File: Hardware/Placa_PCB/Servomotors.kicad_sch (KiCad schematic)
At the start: 12 parts, among them J4 Conn_01x03_Pin, J5 Conn_01x03_Pin, J6 Conn_01x03_Pin, J7 Conn_01x03_Pin

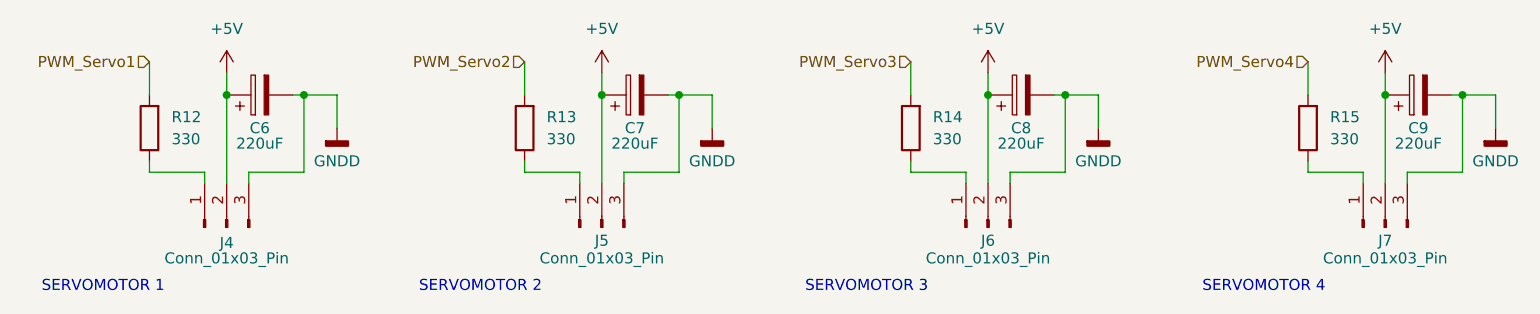
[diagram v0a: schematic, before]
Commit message: Agregando MCU al esquematico
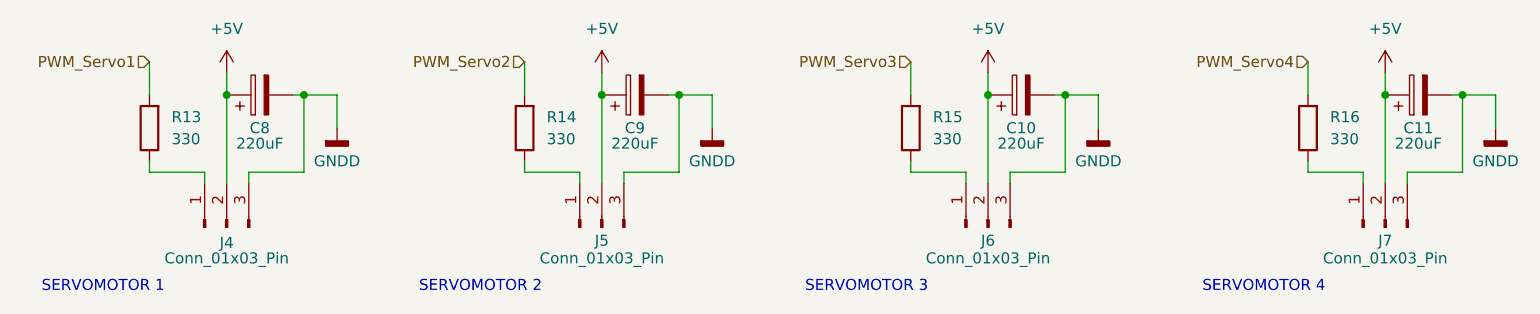
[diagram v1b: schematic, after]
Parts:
- renumbered C8 to C10, C9 to C11, C6 to C8, C7 to C9, R12 to R13, R13 to R14, R14 to R15, R15 to R16
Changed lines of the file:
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@@
+		(dnp no)
+		(fields_autoplaced yes)
+		(property "Reference" "R15"
+			(at 158.75 86.3599 0)
+			(effects
+				(font
+					(size 1.27 1.27)
+				)
+				(justify right)
+			)
+		)
+		(property "Value" "330"
+			(at 158.75 88.8999 0)
+			(effects
+				(font
+					(size 1.27 1.27)
+				)
+				(justify right)
+			)
+		)
+		(property "Footprint" "Resistor_SMD:R_0805_2012Metric_Pad1.20x1.40mm_HandSolder"
+			(at 157.988 87.63 90)
+			(effects
+				(font
+					(size 1.27 1.27)
+				)
+				(hide yes)
+			)
+		)
+		(property "Datasheet" "~"
+			(at 156.21 87.63 0)
+			(effects
+				(font
+					(size 1.27 1.27)
+				)
+				(hide yes)
+			)
+		)
+		(property "Description" "Resistor"
+			(at 156.21 87.63 0)
+			(effects
+				(font
+					(size 1.27 1.27)
+				)
+				(hide yes)
+			)
+		)
+		(pin "1"
+		)
+		(pin "2"
+		)
+		(instances
+			(project "ScramblerBot"
+				(path "/ca162c4b-e7f6-494c-9ea1-0d86ef4a8e44/0bfdb5c0-68d8-49ec-ac8d-698a51ef3bdb"
+					(reference "R15")
+					(unit 1)
+				)
+			)
+		)
+	)
+	(symbol
+		(lib_id "Device:R")
+		(at 201.93 87.63 180)
+		(unit 1)
+		(exclude_from_sim no)
+		(in_bom yes)
+		(on_board yes)
+		(dnp no)
+		(fields_autoplaced yes)
+		(property "Reference" "R16"
+			(at 204.47 86.3599 0)
+			(effects
+				(font
+					(size 1.27 1.27)
+				)
+				(justify right)
+			)
+		)
+		(property "Value" "330"
+			(at 204.47 88.8999 0)
+			(effects
+				(font
+					(size 1.27 1.27)
+				)
+				(justify right)
+			)
+		)
+		(property "Footprint" "Resistor_SMD:R_0805_2012Metric_Pad1.20x1.40mm_HandSolder"
+			(at 203.708 87.63 90)
+			(effects
+				(font
+					(size 1.27 1.27)
+				)
+				(hide yes)
+			)
+		)
+		(property "Datasheet" "~"
+			(at 201.93 87.63 0)
+			(effects
+				(font
+					(size 1.27 1.27)
+				)
+				(hide yes)
+			)
+		)
+		(property "Description" "Resistor"
+			(at 201.93 87.63 0)
+			(effects
+				(font
+					(size 1.27 1.27)
+				)
+				(hide yes)
+			)
+		)
+		(pin "1"
+		)
+		(pin "2"
+		)
+		(instances
+			(project "ScramblerBot"
+				(path "/ca162c4b-e7f6-494c-9ea1-0d86ef4a8e44/0bfdb5c0-68d8-49ec-ac8d-698a51ef3bdb"
+					(reference "R16")
+					(unit 1)
+				)
+			)
+		)
+	)
+	(symbol
+		(lib_id "Device:C_Polarized")
+		(at 214.63 83.82 90)
+		(unit 1)
+		(exclude_from_sim no)
+		(in_bom yes)
+		(on_board yes)
+		(dnp no)
+		(property "Reference" "C11"
+			(at 214.63 87.63 90)
+			(effects
+				(font
+					(size 1.27 1.27)
+				)
+			)
+		)
+		(property "Value" "220uF"
+			(at 214.63 89.408 90)
+			(effects
+				(font
+					(size 1.27 1.27)
+				)
+			)
+		)
+		(property "Footprint" "Capacitor_SMD:CP_Elec_6.3x7.7"
+			(at 218.44 82.8548 0)
+			(effects
+				(font
+					(size 1.27 1.27)
+				)
+				(hide yes)
+			)
+		)
+		(property "Datasheet" "~"
+			(at 214.63 83.82 0)
+			(effects
+				(font
+					(size 1.27 1.27)
+				)
+				(hide yes)
+			)
+		)
+		(property "Description" "Polarized capacitor"
+			(at 214.63 83.82 0)
+			(effects
+				(font
+					(size 1.27 1.27)
+				)
+				(hide yes)
+			)
+		)
+		(pin "1"
+		)
+		(pin "2"
+		)
+		(instances
+			(project "ScramblerBot"
+				(path "/ca162c4b-e7f6-494c-9ea1-0d86ef4a8e44/0bfdb5c0-68d8-49ec-ac8d-698a51ef3bdb"
+					(reference "C11")
+					(unit 1)
+				)
+			)
+		)
+	)
+	(symbol
+		(lib_id "Device:R")
+		(at 111.76 87.63 180)
+		(unit 1)
+		(exclude_from_sim no)
+		(in_bom yes)
+		(on_board yes)
 		(dnp no)
 		(fields_autoplaced yes)
 		(property "Reference" "R14"
-			(at 158.75 86.3599 0)
-			(effects
-				(font
-					(size 1.27 1.27)
-				)
-				(justify right)
-			)
-		)
-		(property "Value" "330"
-			(at 158.75 88.8999 0)
-			(effects
-				(font
-					(size 1.27 1.27)
-				)
-				(justify right)
-			)
-		)
-		(property "Footprint" "Resistor_SMD:R_0805_2012Metric_Pad1.20x1.40mm_HandSolder"
-			(at 157.988 87.63 90)
-			(effects
-				(font
-					(size 1.27 1.27)
-				)
-				(hide yes)
-			)
-		)
-		(property "Datasheet" "~"
-			(at 156.21 87.63 0)
-			(effects
-				(font
-					(size 1.27 1.27)
-				)
-				(hide yes)
-			)
-		)
-		(property "Description" "Resistor"
-			(at 156.21 87.63 0)
-			(effects
-				(font
-					(size 1.27 1.27)
-				)
-				(hide yes)
-			)
-		)
-		(pin "1"
-		)
-		(pin "2"
-		)
-		(instances
-			(project "ScramblerBot"
-				(path "/ca162c4b-e7f6-494c-9ea1-0d86ef4a8e44/0bfdb5c0-68d8-49ec-ac8d-698a51ef3bdb"
-					(reference "R14")
-					(unit 1)
-				)
-			)
-		)
-	)
-	(symbol
-		(lib_id "Device:R")
-		(at 201.93 87.63 180)
-		(unit 1)
-		(exclude_from_sim no)
-		(in_bom yes)
-		(on_board yes)
-		(dnp no)
-		(fields_autoplaced yes)
-		(property "Reference" "R15"
-			(at 204.47 86.3599 0)
-			(effects
-				(font
-					(size 1.27 1.27)
-				)
-				(justify right)
-			)
-		)
-		(property "Value" "330"
-			(at 204.47 88.8999 0)
-			(effects
-				(font
-					(size 1.27 1.27)
-				)
-				(justify right)
-			)
-		)
-		(property "Footprint" "Resistor_SMD:R_0805_2012Metric_Pad1.20x1.40mm_HandSolder"
-			(at 203.708 87.63 90)
-			(effects
-				(font
-					(size 1.27 1.27)
-				)
-				(hide yes)
-			)
-		)
-		(property "Datasheet" "~"
-			(at 201.93 87.63 0)
-			(effects
-				(font
-					(size 1.27 1.27)
-				)
-				(hide yes)
-			)
-		)
-		(property "Description" "Resistor"
-			(at 201.93 87.63 0)
-			(effects
-				(font
-					(size 1.27 1.27)
-				)
-				(hide yes)
-			)
-		)
-		(pin "1"
-		)
-		(pin "2"
-		)
-		(instances
-			(project "ScramblerBot"
-				(path "/ca162c4b-e7f6-494c-9ea1-0d86ef4a8e44/0bfdb5c0-68d8-49ec-ac8d-698a51ef3bdb"
-					(reference "R15")
-					(unit 1)
-				)
-			)
-		)
-	)
-	(symbol
-		(lib_id "Device:C_Polarized")
-		(at 214.63 83.82 90)
-		(unit 1)
-		(exclude_from_sim no)
-		(in_bom yes)
-		(on_board yes)
-		(dnp no)
-		(property "Reference" "C9"
-			(at 214.63 87.63 90)
-			(effects
-				(font
-					(size 1.27 1.27)
-				)
-			)
-		)
-		(property "Value" "220uF"
-			(at 214.63 89.408 90)
-			(effects
-				(font
-					(size 1.27 1.27)
-				)
-			)
-		)
-		(property "Footprint" "Capacitor_SMD:CP_Elec_6.3x7.7"
-			(at 218.44 82.8548 0)
-			(effects
-				(font
-					(size 1.27 1.27)
-				)
-				(hide yes)
-			)
-		)
-		(property "Datasheet" "~"
-			(at 214.63 83.82 0)
-			(effects
-				(font
-					(size 1.27 1.27)
-				)
-				(hide yes)
-			)
-		)
-		(property "Description" "Polarized capacitor"
-			(at 214.63 83.82 0)
-			(effects
-				(font
-					(size 1.27 1.27)
-				)
-				(hide yes)
-			)
-		)
-		(pin "1"
-		)
-		(pin "2"
-		)
-		(instances
-			(project "ScramblerBot"
-				(path "/ca162c4b-e7f6-494c-9ea1-0d86ef4a8e44/0bfdb5c0-68d8-49ec-ac8d-698a51ef3bdb"
-					(reference "C9")
-					(unit 1)
-				)
-			)
-		)
-	)
-	(symbol
-		(lib_id "Device:R")
-		(at 111.76 87.63 180)
-		(unit 1)
-		(exclude_from_sim no)
-		(in_bom yes)
-		(on_board yes)
-		(dnp no)
-		(fields_autoplaced yes)
-		(property "Reference" "R13"
 			(at 114.3 86.3599 0)
 			(effects
@@
 			(project "ScramblerBot"
 				(path "/ca162c4b-e7f6-494c-9ea1-0d86ef4a8e44/0bfdb5c0-68d8-49ec-ac8d-698a51ef3bdb"
-					(reference "R13")
+					(reference "R14")
 					(unit 1)
 				)
@@
 		(on_board yes)
 		(dnp no)
-		(property "Reference" "C8"
+		(property "Reference" "C10"
 			(at 168.91 87.63 90)
 			(effects
@@
 			(project "ScramblerBot"
 				(path "/ca162c4b-e7f6-494c-9ea1-0d86ef4a8e44/0bfdb5c0-68d8-49ec-ac8d-698a51ef3bdb"
-					(reference "C8")
+					(reference "C10")
 					(unit 1)
 				)
@@
 		(on_board yes)
 		(dnp no)
-		(property "Reference" "C7"
+		(property "Reference" "C9"
 			(at 124.46 87.63 90)
 			(effects
@@
 			(project "ScramblerBot"
 				(path "/ca162c4b-e7f6-494c-9ea1-0d86ef4a8e44/0bfdb5c0-68d8-49ec-ac8d-698a51ef3bdb"
-					(reference "C7")
+					(reference "C9")
 					(unit 1)
 				)
@@
 		(on_board yes)
 		(dnp no)
-		(property "Reference" "C6"
+		(property "Reference" "C8"
 			(at 81.28 87.63 90)
 			(effects
@@
 			(project ""
 				(path "/ca162c4b-e7f6-494c-9ea1-0d86ef4a8e44/0bfdb5c0-68d8-49ec-ac8d-698a51ef3bdb"
-					(reference "C6")
+					(reference "C8")
 					(unit 1)
 				)
@@
 		(dnp no)
 		(fields_autoplaced yes)
-		(property "Reference" "R12"
+		(property "Reference" "R13"
 			(at 71.12 86.3599 0)
 			(effects
@@
 			(project ""
 				(path "/ca162c4b-e7f6-494c-9ea1-0d86ef4a8e44/0bfdb5c0-68d8-49ec-ac8d-698a51ef3bdb"
-					(reference "R12")
-					(unit 1)
-				)
+					(reference "R13")
+					(unit 1)
+				)

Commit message: Esquematico Final
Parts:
- C10, C11, C8, C9: footprint Capacitor_SMD:CP_Elec_6.3x7.7 -> Capacitor_SMD:CP_Elec_8x6.2
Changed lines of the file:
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@@
 			)
 		)
-		(property "Footprint" "Capacitor_SMD:CP_Elec_6.3x7.7"
+		(property "Footprint" "Capacitor_SMD:CP_Elec_8x6.2"
 			(at 218.44 82.8548 0)
 			(effects
@@
 			)
 		)
-		(property "Footprint" "Capacitor_SMD:CP_Elec_6.3x7.7"
+		(property "Footprint" "Capacitor_SMD:CP_Elec_8x6.2"
 			(at 172.72 82.8548 0)
 			(effects
@@
 			)
 		)
-		(property "Footprint" "Capacitor_SMD:CP_Elec_6.3x7.7"
+		(property "Footprint" "Capacitor_SMD:CP_Elec_8x6.2"
 			(at 128.27 82.8548 0)
 			(effects
@@
 			)
 		)
-		(property "Footprint" "Capacitor_SMD:CP_Elec_6.3x7.7"
+		(property "Footprint" "Capacitor_SMD:CP_Elec_8x6.2"
 			(at 85.09 82.8548 0)
 			(effects
